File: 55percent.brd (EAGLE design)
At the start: 255.3 x 102.9 mm, 145 parts, among them J1 USB4085-GF-A_REVA, U1 ATMEGA32A-PU

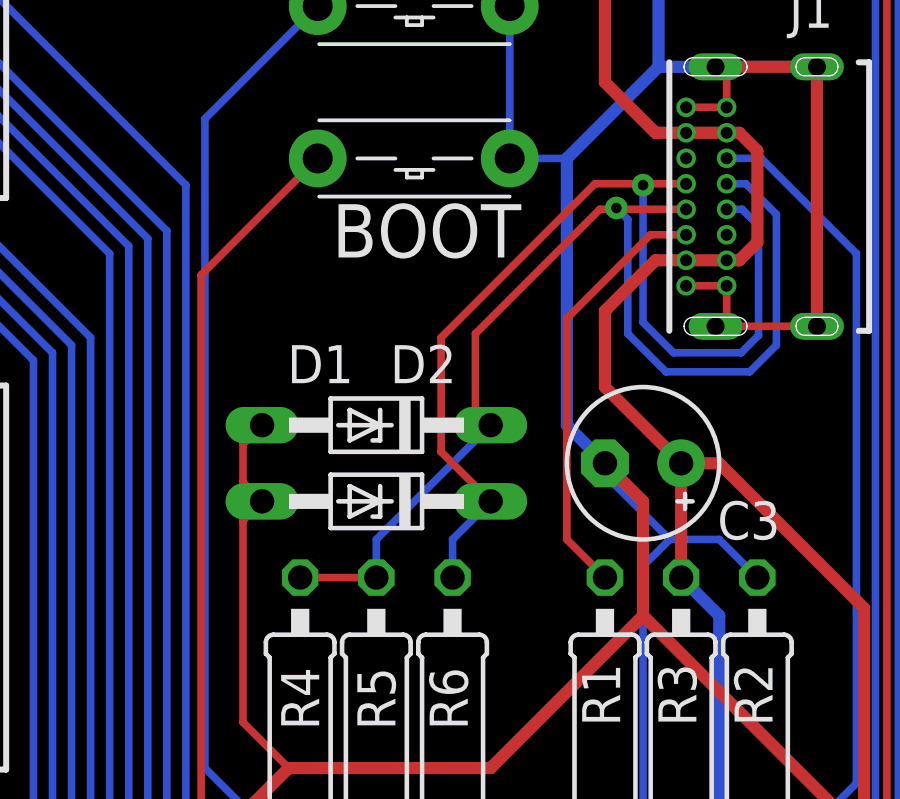
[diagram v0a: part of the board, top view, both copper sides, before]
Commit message: Fixed Resistor Placement
If you have used a prior version of any of these files, contact me
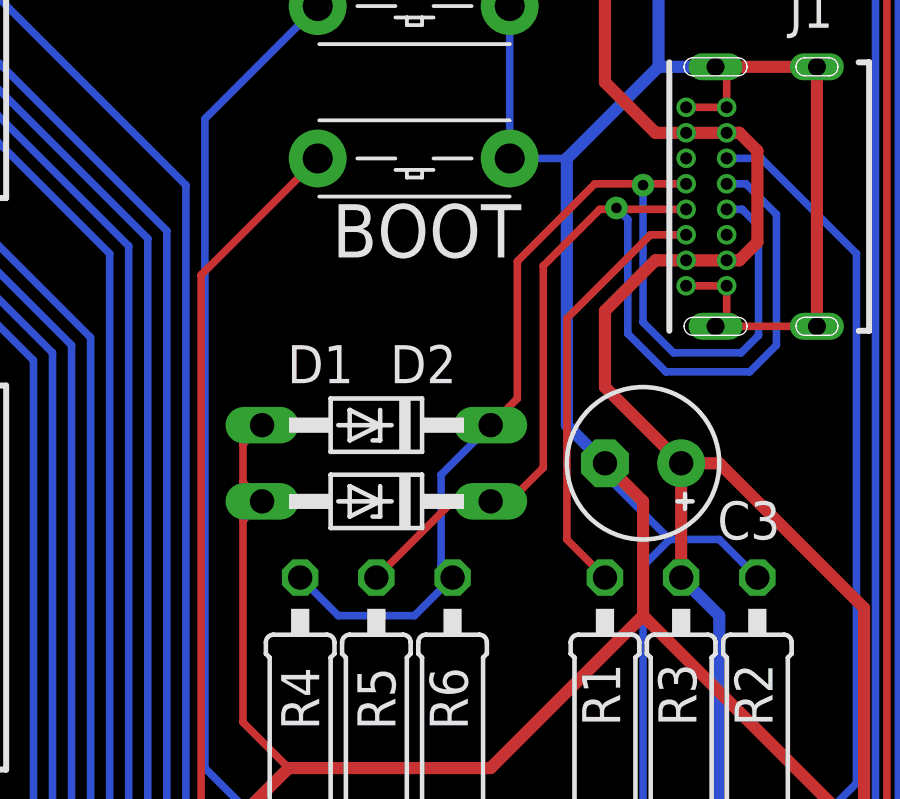
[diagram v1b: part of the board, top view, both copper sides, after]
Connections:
- net N$3: now also D1.C; no longer D2.C, R4.2
- net N$7: now also D2.C, R4.2; no longer D1.C
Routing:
- net N$7: track 33.6 -> 38.7 mm
- net N$3: track 37.9 -> 36.1 mm
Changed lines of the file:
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@@
 <setting verticaltext="up"/>
 </settings>
-<grid distance="50" unitdist="mil" unit="mil" style="lines" multiple="3" display="yes" altdistance="5" altunitdist="mil" altunit="mil"/>
+<grid distance="50" unitdist="mil" unit="mil" style="lines" multiple="3" display="no" altdistance="5" altunitdist="mil" altunit="mil"/>
 <layers>
 <layer number="1" name="Top" color="4" fill="1" visible="yes" active="yes"/>
@@
 </signal>
 <signal name="N$3">
-<contactref element="D2" pad="C"/>
 <contactref element="R5" pad="2"/>
-<wire x1="236.22" y1="69.85" x2="236.22" y2="71.12" width="0.254" layer="16"/>
-<wire x1="236.22" y1="71.12" x2="240.03" y2="74.93" width="0.254" layer="16"/>
-<wire x1="239.522" y1="77.978" x2="239.522" y2="75.438" width="0.254" layer="1"/>
-<wire x1="240.03" y1="74.93" x2="239.522" y2="75.438" width="0.254" layer="1"/>
 <wire x1="243.669" y1="82.125" x2="244.177" y2="82.125" width="0.254" layer="1"/>
 <wire x1="244.177" y1="82.125" x2="246.546" y2="82.125" width="0.254" layer="1"/>
-<wire x1="239.522" y1="77.978" x2="243.669" y2="82.125" width="0.254" layer="1"/>
 <via x="244.221" y="82.169" extent="1-16" drill="0.35"/>
 <wire x1="244.221" y1="82.169" x2="244.602" y2="81.788" width="0.254" layer="16"/>
@@
 <contactref element="J1" pad="A6"/>
 <contactref element="J1" pad="B6"/>
-<contactref element="R4" pad="2"/>
 <wire x1="244.221" y1="82.169" x2="244.177" y2="82.125" width="0.254" layer="1"/>
-<wire x1="233.68" y1="69.85" x2="236.22" y2="69.85" width="0.254" layer="1"/>
+<contactref element="D1" pad="C"/>
+<wire x1="241.7826" y1="80.2386" x2="241.7826" y2="73.5076" width="0.254" layer="1"/>
+<wire x1="240.03" y1="72.39" x2="240.665" y2="72.39" width="0.254" layer="1"/>
+<wire x1="240.665" y1="72.39" x2="241.7826" y2="73.5076" width="0.254" layer="1"/>
+<wire x1="240.03" y1="72.39" x2="238.76" y2="72.39" width="0.254" layer="1"/>
+<wire x1="238.76" y1="72.39" x2="236.22" y2="69.85" width="0.254" layer="1"/>
+<wire x1="241.7826" y1="80.2386" x2="243.669" y2="82.125" width="0.254" layer="1"/>
 </signal>
 <signal name="D+">
@@
 <signal name="N$7">
 <contactref element="R6" pad="2"/>
-<contactref element="D1" pad="C"/>
-<wire x1="240.03" y1="72.39" x2="238.379" y2="74.041" width="0.254" layer="1"/>
-<wire x1="238.379" y1="74.041" x2="238.379" y2="77.851" width="0.254" layer="1"/>
-<wire x1="238.379" y1="77.851" x2="243.503" y2="82.975" width="0.254" layer="1"/>
+<wire x1="240.919" y1="80.391" x2="243.503" y2="82.975" width="0.254" layer="1"/>
 <wire x1="243.503" y1="82.975" x2="245.11" y2="82.975" width="0.254" layer="1"/>
 <via x="245.11" y="82.931" extent="1-16" drill="0.35"/>
@@
 <wire x1="248.9594" y1="77.92286875" x2="248.9594" y2="81.57718125" width="0.254" layer="16"/>
 <wire x1="246.126" y1="77.343" x2="248.37953125" y2="77.343" width="0.254" layer="16"/>
-<wire x1="238.76" y1="69.85" x2="238.76" y2="71.12" width="0.254" layer="16"/>
-<wire x1="238.76" y1="71.12" x2="240.03" y2="72.39" width="0.254" layer="16"/>
 <contactref element="J1" pad="A7"/>
 <contactref element="J1" pad="B7"/>
 <wire x1="245.11" y1="82.931" x2="245.11" y2="82.975" width="0.254" layer="1"/>
+<contactref element="D2" pad="C"/>
+<contactref element="R4" pad="2"/>
+<wire x1="240.919" y1="80.391" x2="240.919" y2="75.819" width="0.254" layer="1"/>
+<wire x1="240.919" y1="75.819" x2="240.03" y2="74.93" width="0.254" layer="1"/>
+<wire x1="233.68" y1="69.85" x2="234.95" y2="68.58" width="0.254" layer="16"/>
+<wire x1="234.95" y1="68.58" x2="237.49" y2="68.58" width="0.254" layer="16"/>
+<wire x1="237.49" y1="68.58" x2="238.76" y2="69.85" width="0.254" layer="16"/>
+<wire x1="238.76" y1="69.85" x2="238.379" y2="70.231" width="0.254" layer="16"/>
+<wire x1="238.379" y1="73.279" x2="240.03" y2="74.93" width="0.254" layer="16"/>
+<wire x1="238.379" y1="70.231" x2="238.379" y2="73.279" width="0.254" layer="16"/>
 </signal>
 <signal name="MISO">
